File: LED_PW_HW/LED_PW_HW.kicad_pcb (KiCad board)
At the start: 2 copper layers, 44 x 44 mm, 146 parts, among them U1 IS31FL3732A

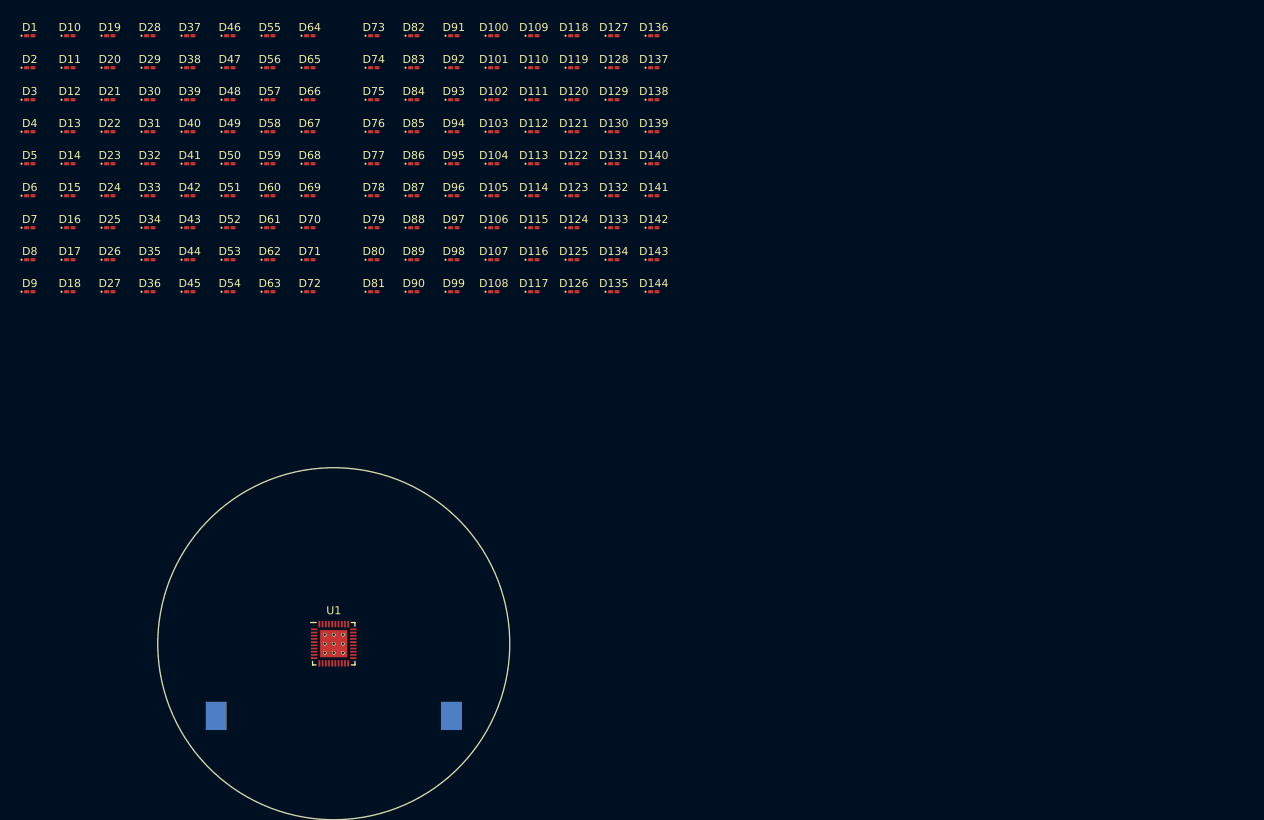
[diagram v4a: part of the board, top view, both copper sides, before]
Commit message: schematic of led driver part done
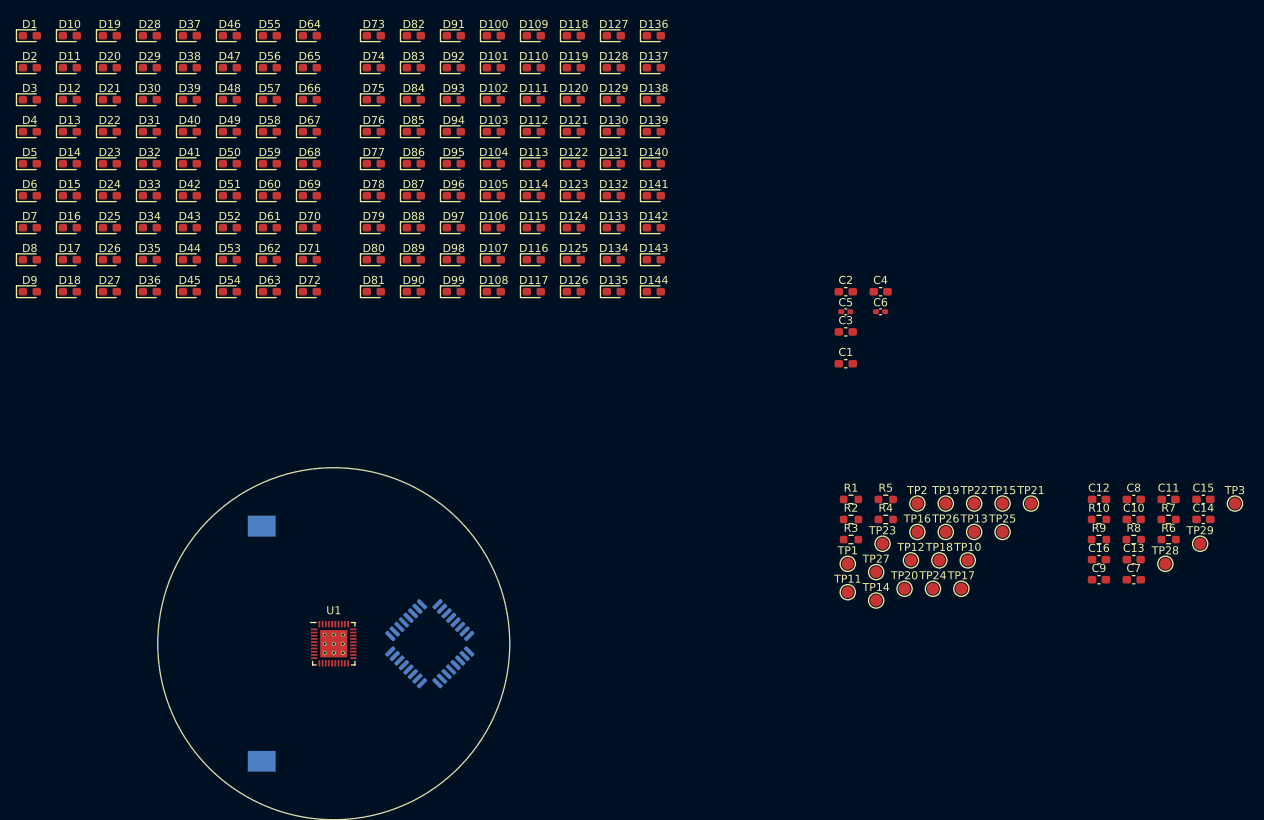
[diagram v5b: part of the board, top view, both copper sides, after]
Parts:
- added C1: 100n, Capacitor_SMD:C_0603_1608Metric_Pad1.08x0.95mm_HandSolder, F.Cu at (204.0, 75.0)
- added C10: 100n, Capacitor_SMD:C_0603_1608Metric_Pad1.08x0.95mm_HandSolder, F.Cu at (240.0, 94.5)
- added C11: 100n n.b., Capacitor_SMD:C_0603_1608Metric_Pad1.08x0.95mm_HandSolder, F.Cu at (244.3, 92.0)
- added C12: 100n n.b., Capacitor_SMD:C_0603_1608Metric_Pad1.08x0.95mm_HandSolder, F.Cu at (235.7, 92.0)
- added C13: 1u, Capacitor_SMD:C_0603_1608Metric_Pad1.08x0.95mm_HandSolder, F.Cu at (240.0, 99.5)
- added C14: 1u n.b., Capacitor_SMD:C_0603_1608Metric_Pad1.08x0.95mm_HandSolder, F.Cu at (248.7, 94.5)
- added C15: 1u n.b., Capacitor_SMD:C_0603_1608Metric_Pad1.08x0.95mm_HandSolder, F.Cu at (248.7, 92.0)
- added C16: 1u n.b., Capacitor_SMD:C_0603_1608Metric_Pad1.08x0.95mm_HandSolder, F.Cu at (235.7, 99.5)
- added C2: 100n, Capacitor_SMD:C_0603_1608Metric_Pad1.08x0.95mm_HandSolder, F.Cu at (204.0, 66.0)
- added C3: 100n, Capacitor_SMD:C_0603_1608Metric_Pad1.08x0.95mm_HandSolder, F.Cu at (204.0, 71.0)
- added C4: 1u, Capacitor_SMD:C_0603_1608Metric_Pad1.08x0.95mm_HandSolder, F.Cu at (208.3, 66.0)
- added C5: 4p3, Capacitor_SMD:C_0402_1005Metric_Pad0.74x0.62mm_HandSolder, F.Cu at (204.0, 68.5)
- added C6: 4p3, Capacitor_SMD:C_0402_1005Metric_Pad0.74x0.62mm_HandSolder, F.Cu at (208.3, 68.5)
- added C7: 100n, Capacitor_SMD:C_0603_1608Metric_Pad1.08x0.95mm_HandSolder, F.Cu at (240.0, 102.0)
- added C8: 220n n.b., Capacitor_SMD:C_0603_1608Metric_Pad1.08x0.95mm_HandSolder, F.Cu at (240.0, 92.0)
- added C9: 100n n.b., Capacitor_SMD:C_0603_1608Metric_Pad1.08x0.95mm_HandSolder, F.Cu at (235.7, 102.0)
- added R1: 100k, Resistor_SMD:R_0603_1608Metric_Pad0.98x0.95mm_HandSolder, F.Cu at (204.7, 92.0)
- added R10: 100k, Resistor_SMD:R_0603_1608Metric_Pad0.98x0.95mm_HandSolder, F.Cu at (235.7, 94.5)
- added R2: 100k, Resistor_SMD:R_0603_1608Metric_Pad0.98x0.95mm_HandSolder, F.Cu at (204.7, 94.5)
- added R3: 100k, Resistor_SMD:R_0603_1608Metric_Pad0.98x0.95mm_HandSolder, F.Cu at (204.7, 97.0)
- added R4: 100k, Resistor_SMD:R_0603_1608Metric_Pad0.98x0.95mm_HandSolder, F.Cu at (209.0, 94.5)
- added R5: n.b., Resistor_SMD:R_0603_1608Metric_Pad0.98x0.95mm_HandSolder, F.Cu at (209.0, 92.0)
- added R6: 20k, Resistor_SMD:R_0603_1608Metric_Pad0.98x0.95mm_HandSolder, F.Cu at (244.3, 97.0)
- added R7: 10k, Resistor_SMD:R_0603_1608Metric_Pad0.98x0.95mm_HandSolder, F.Cu at (244.3, 94.5)
- added R8: 100k, Resistor_SMD:R_0603_1608Metric_Pad0.98x0.95mm_HandSolder, F.Cu at (240.0, 97.0)
- added R9: 10k, Resistor_SMD:R_0603_1608Metric_Pad0.98x0.95mm_HandSolder, F.Cu at (235.7, 97.0)
- added TP1: TestPoint, TestPoint:TestPoint_Pad_D1.5mm, F.Cu at (204.2, 100.0)
- added TP10: TestPoint, TestPoint:TestPoint_Pad_D1.5mm, F.Cu at (219.2, 99.6)
- added TP11: TestPoint, TestPoint:TestPoint_Pad_D1.5mm, F.Cu at (204.2, 103.6)
- added TP12: TestPoint, TestPoint:TestPoint_Pad_D1.5mm, F.Cu at (212.2, 99.6)
- added TP13: TestPoint, TestPoint:TestPoint_Pad_D1.5mm, F.Cu at (220.1, 96.0)
- added TP14: TestPoint, TestPoint:TestPoint_Pad_D1.5mm, F.Cu at (207.8, 104.6)
- added TP15: TestPoint, TestPoint:TestPoint_Pad_D1.5mm, F.Cu at (223.6, 92.5)
- added TP16: TestPoint, TestPoint:TestPoint_Pad_D1.5mm, F.Cu at (212.9, 96.0)
- added TP17: TestPoint, TestPoint:TestPoint_Pad_D1.5mm, F.Cu at (218.4, 103.1)
- added TP18: TestPoint, TestPoint:TestPoint_Pad_D1.5mm, F.Cu at (215.7, 99.6)
- added TP19: TestPoint, TestPoint:TestPoint_Pad_D1.5mm, F.Cu at (216.5, 92.5)
- added TP2: TestPoint, TestPoint:TestPoint_Pad_D1.5mm, F.Cu at (212.9, 92.5)
- added TP20: TestPoint, TestPoint:TestPoint_Pad_D1.5mm, F.Cu at (211.3, 103.1)
- added TP21: TestPoint, TestPoint:TestPoint_Pad_D1.5mm, F.Cu at (227.2, 92.5)
- added TP22: TestPoint, TestPoint:TestPoint_Pad_D1.5mm, F.Cu at (220.1, 92.5)
- added TP23: TestPoint, TestPoint:TestPoint_Pad_D1.5mm, F.Cu at (208.6, 97.5)
- added TP24: TestPoint, TestPoint:TestPoint_Pad_D1.5mm, F.Cu at (214.9, 103.1)
- added TP25: TestPoint, TestPoint:TestPoint_Pad_D1.5mm, F.Cu at (223.6, 96.0)
- added TP26: TestPoint, TestPoint:TestPoint_Pad_D1.5mm, F.Cu at (216.5, 96.0)
- added TP27: TestPoint, TestPoint:TestPoint_Pad_D1.5mm, F.Cu at (207.8, 101.0)
- added TP28: TestPoint, TestPoint:TestPoint_Pad_D1.5mm, F.Cu at (243.9, 100.0)
- added TP29: TestPoint, TestPoint:TestPoint_Pad_D1.5mm, F.Cu at (248.3, 97.5)
- added TP3: TestPoint, TestPoint:TestPoint_Pad_D1.5mm, F.Cu at (252.7, 92.5)
- added U2: STM32L031K6Tx, Package_QFP:LQFP-32_7x7mm_P0.8mm, B.Cu at (152.0, 110.0)
- D1, D10, D100, D101, D102, D103, D104, D105, D106, D107, D108, D109, D11, D110, D111, D112, D113, D114, D115, D116, D117, D118, D119, D12, D120, D121, D122, D123, D124, D125, D126, D127, D128, D129, D13, D130, D131, D132, D133, D134, D135, D136, D137, D138, D139, D14, D140, D141, D142, D143, D144, D15, D16, D17, D18, D19, D2, D20, D21, D22, D23, D24, D25, D26, D27, D28, D29, D3, D30, D31, D32, D33, D34, D35, D36, D37, D38, D39, D4, D40, D41, D42, D43, D44, D45, D46, D47, D48, D49, D5, D50, D51, D52, D53, D54, D55, D56, D57, D58, D59, D6, D60, D61, D62, D63, D64, D65, D66, D67, D68, D69, D7, D70, D71, D72, D73, D74, D75, D76, D77, D78, D79, D8, D80, D81, D82, D83, D84, D85, D86, D87, D88, D89, D9, D90, D91, D92, D93, D94, D95, D96, D97, D98, D99: footprint LED_SMD:LED_0201_0603Metric_Pad0.64x0.40mm_HandSolder -> LED_SMD:LED_0603_1608Metric_Pad1.05x0.95mm_HandSolder
- moved BT1 12.7 mm to (131.0, 110.0), turned to -90 degrees
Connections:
- BT1 pad 1: unconnected-(BT1-Pad1) -> +3V3
- BT1 pad 2: unconnected-(BT1-Pad2) -> GND
- U1 pad 1: unconnected-(U1-Pad1) -> +3V3
- U1 pad 20: unconnected-(U1-Pad20) -> +3V3
- U1 pad 21: unconnected-(U1-Pad21) -> I2C_SDA
- U1 pad 22: unconnected-(U1-Pad22) -> I2C_SCL
- U1 pad 23: unconnected-(U1-Pad23) -> GND
- U1 pad 24: unconnected-(U1-Pad24) -> GND
- U1 pad 25: unconnected-(U1-Pad25) -> LED_EN
- U1 pad 26: unconnected-(U1-Pad26) -> +3V3
- U1 pad 27: unconnected-(U1-Pad27) -> +3V3
- U1 pad 28: unconnected-(U1-Pad28) -> R_EXT
- U1 pad 29: unconnected-(U1-Pad29) -> C_FILT
- U1 pad 4: unconnected-(U1-Pad4) -> +3V3
- U1 pad 5: unconnected-(U1-Pad5) -> INTB
- U1 pad 6: unconnected-(U1-Pad6) -> AUDIO_IN

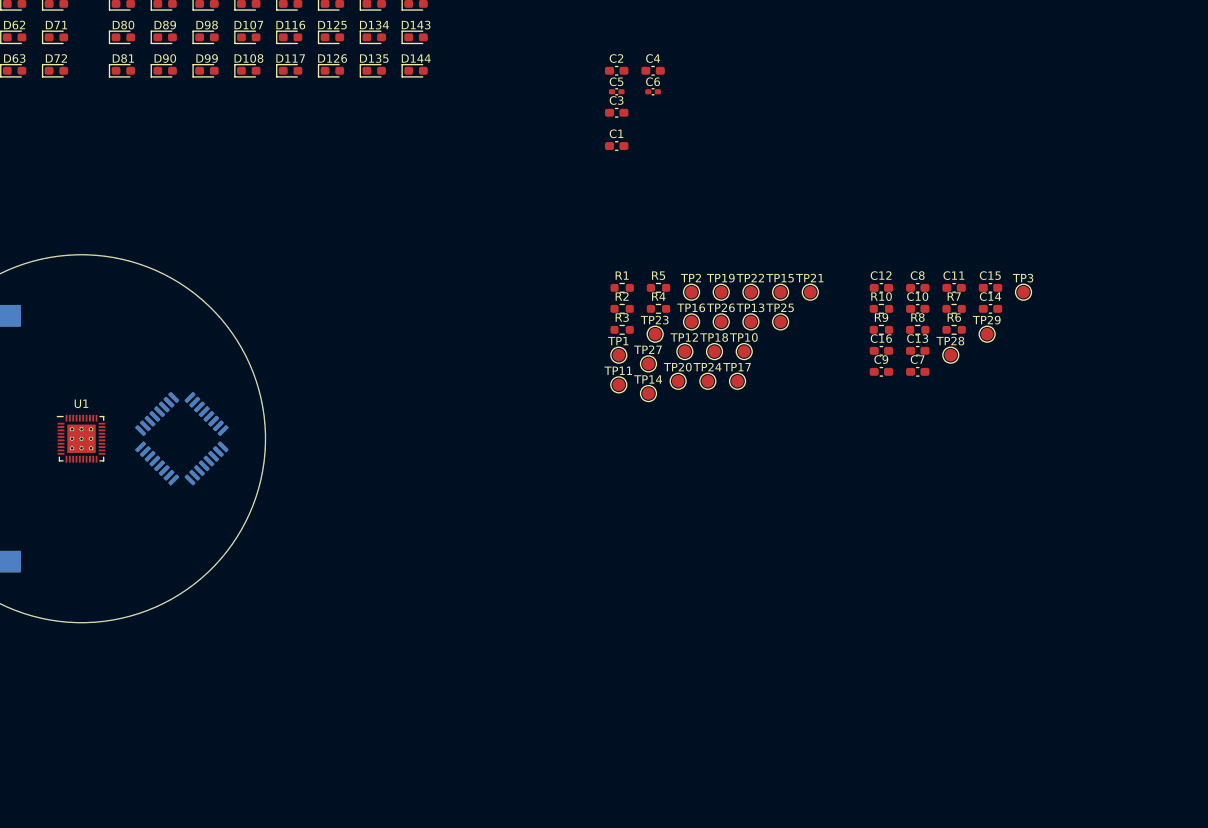
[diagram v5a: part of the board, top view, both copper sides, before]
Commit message: controller schematic part done
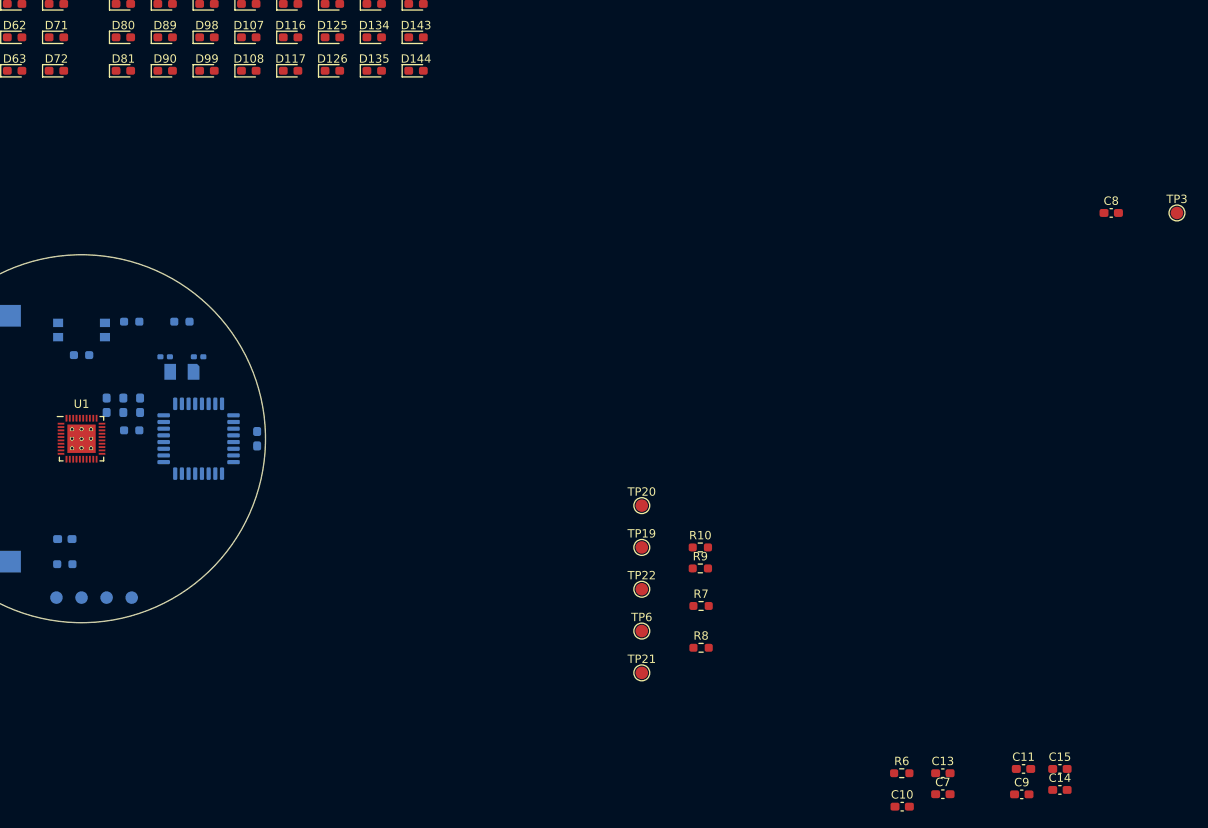
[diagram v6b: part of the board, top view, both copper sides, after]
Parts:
- removed C16: 1u n.b., Capacitor_SMD:C_0603_1608Metric_Pad1.08x0.95mm_HandSolder
- removed TP10, TP11, TP12, TP13, TP14, TP15, TP16, TP17, TP18, TP23, TP24, TP25, TP26, TP27, TP28, TP29: TestPoint, TestPoint:TestPoint_Pad_D1.5mm
- added SW1: SW_MEC_5E, LED_PW_HW_Library:Switch-DifferentPadNr, B.Cu at (140.0, 97.0)
- added TP4: TestPoint, TestPoint:TestPoint_Pad_D1.5mm, B.Cu at (140.0, 129.0)
- added TP5: TestPoint, TestPoint:TestPoint_Pad_D1.5mm, B.Cu at (143.0, 129.0)
- added TP6: TestPoint, TestPoint:TestPoint_Pad_D1.5mm, F.Cu at (207.0, 133.0)
- added Y1: Crystal, LED_PW_HW_Library:ECX-34Q, B.Cu at (152.0, 102.0)
- C1, C12, C2, C3, C4, C5, C6, R1, R2, R3, R4, R5, TP1, TP2: moved to B.Cu
- moved C12 93.7 mm to (143.0, 106.0), turned to -90 degrees
- moved C3 83.4 mm to (138.0, 122.0), turned to 180 degrees
- moved TP2 76.3 mm to (146.0, 129.0), turned to 180 degrees
- moved C4 74.9 mm to (145.0, 106.0), turned to -90 degrees
- moved R1 74.4 mm to (138.0, 125.0), turned to 180 degrees
- moved TP1 73.2 mm to (137.0, 129.0), turned to 180 degrees
- moved R5 69.5 mm to (140.0, 100.0)
- moved C1 64.9 mm to (147.0, 106.0), turned to -90 degrees
- moved R4 63.0 mm to (146.0, 96.0), turned to 180 degrees
- moved C6 62.9 mm to (154.0, 100.2)
- moved C5 62.6 mm to (150.0, 100.2), turned to 180 degrees
- moved C2 61.5 mm to (161.0, 110.0), turned to 90 degrees
- moved R2 60.4 mm to (146.0, 109.0), turned to 180 degrees
- moved C10 59.6 mm to (238.1, 154.0)
- moved C11 58.1 mm to (252.7, 149.5)
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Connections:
- TP2 pad 1: BOOT -> SWDIO
- U2 pad 10: PA4 -> unconnected-(U2-Pad10)
- U2 pad 11: PA5 -> unconnected-(U2-Pad11)
- U2 pad 12: PA6 -> unconnected-(U2-Pad12)
- U2 pad 13: PA7 -> unconnected-(U2-Pad13)
- U2 pad 18: PA8 -> INTB
- U2 pad 23: PA13 -> SWDIO
- U2 pad 24: PA14 -> SWCLK
- U2 pad 25: PA15 -> unconnected-(U2-Pad25)
- U2 pad 8: PA2 -> unconnected-(U2-Pad8)
- U2 pad 9: PA3 -> unconnected-(U2-Pad9)

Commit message: led placement
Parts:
- moved D141 196.7 mm to (-9.44, 1.05), turned to 6.35714 degrees
- moved D140 194.7 mm to (-8.97, 3.13), turned to 19.2143 degrees
- moved D139 192.5 mm to (-8.05, 5.04), turned to 32.0714 degrees
- moved D129 192.1 mm to (-12.9, 1.81), turned to 8 degrees
- moved D128 190.6 mm to (-12.5, 3.58), turned to 16 degrees
- moved D126 190.4 mm to (-11.0, 6.89), turned to 32 degrees
- moved D138 190.0 mm to (-6.73, 6.71), turned to 44.9286 degrees
- moved D130 189.2 mm to (-6.72, -6.72), turned to -45 degrees
- moved D127 189.1 mm to (-11.9, 5.29), turned to 24 degrees
- moved D131 188.1 mm to (-3.64, -8.78), turned to -67.5 degrees
- moved D125 187.8 mm to (-9.96, 8.36), turned to 40 degrees
- moved D137 187.5 mm to (-5.06, 8.04), turned to 57.7857 degrees
- moved D117 187.2 mm to (-8.78, -3.64), turned to -22.5 degrees
- moved D132 186.2 mm to (0.00, -9.50), turned to -90 degrees
- moved D124 185.1 mm to (-8.70, 9.66), turned to 48 degrees
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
